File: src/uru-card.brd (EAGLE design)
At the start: 54 x 85.6 mm, 46 parts, among them U1 ESP32-PICO-D4, U2 MPR121QR2, U3 AP2112K-3.3TRG1, U4 FT260Q-T, U6 ATECC508A-UDFN

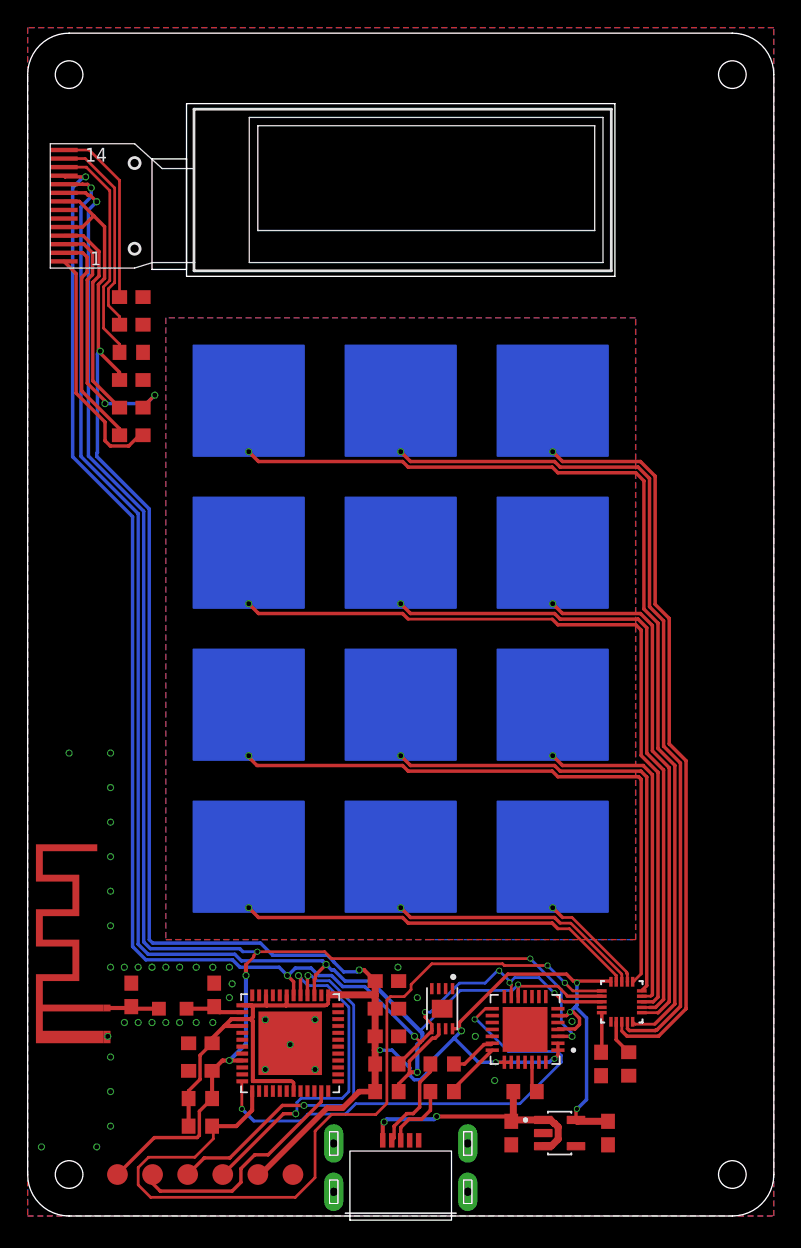
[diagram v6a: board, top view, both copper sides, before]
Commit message: Fixed incorrect connections
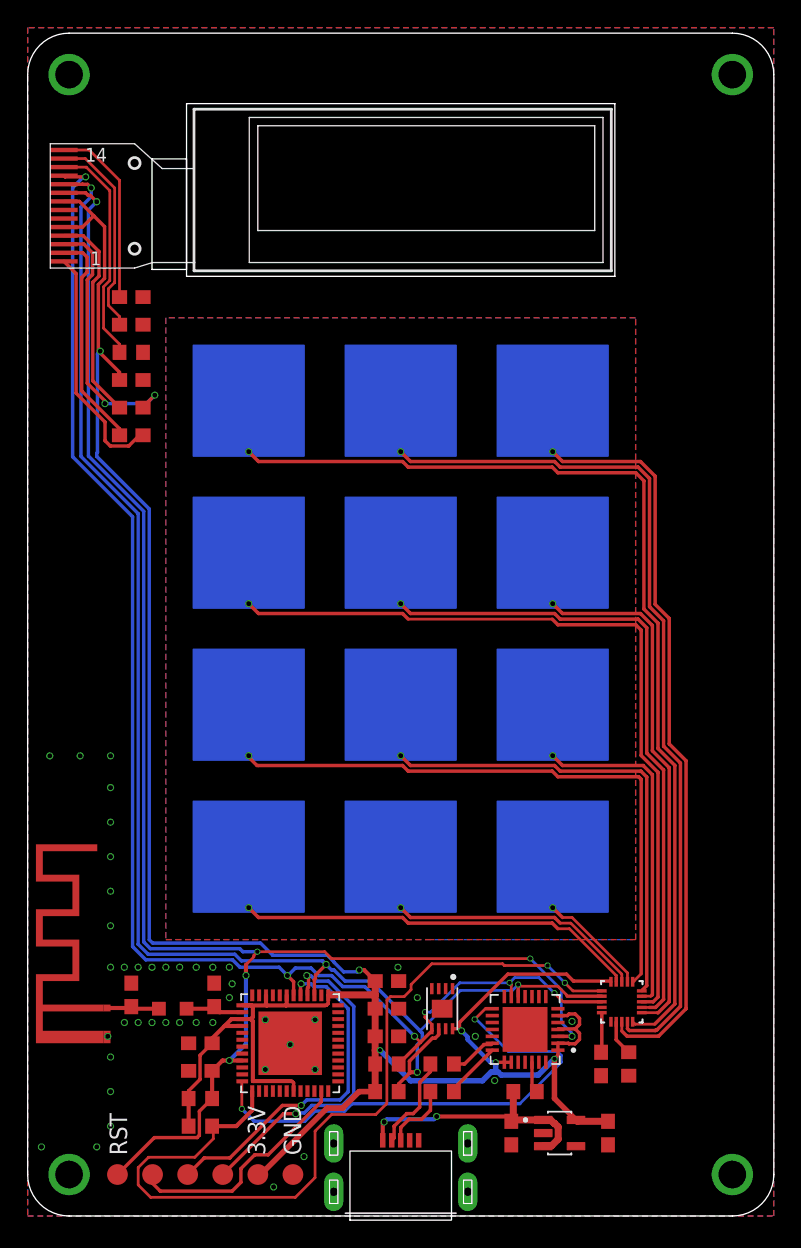
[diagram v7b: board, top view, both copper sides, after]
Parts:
- R2: value 10K -> 75K
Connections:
- net RXD: now also U1.41; no longer U1.40
- net TXD: now also U1.40; no longer U1.41
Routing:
- net +3V3: track 183.2 -> 181.2 mm, vias 9 -> 6
- net RXD: track 26.7 -> 25.1 mm
- net SDA: track 106.7 -> 105.9 mm, vias 7 -> 6
- net GND: vias 41 -> 48
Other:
- board text added: "3.3V"
- board text added: "GND"
- board text added: "RST"
